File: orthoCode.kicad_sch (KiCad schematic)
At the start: 160 parts, among them K1:1 KEYSW, K1:10 KEYSW, K1:11 KEYSW, K1:12 KEYSW, K1:13 KEYSW, K1:14 KEYSW, K1:2 KEYSW, K1:3 KEYSW, K1:4 KEYSW, K1:5 KEYSW, K1:6 KEYSW, K1:7 KEYSW, K1:8 KEYSW, K1:9 KEYSW, K2:1 KEYSW, K2:10 KEYSW, K2:11 KEYSW, K2:13 KEYSW, K2:2 KEYSW, K2:3 KEYSW, K2:4 KEYSW, K2:5 KEYSW, K2:6 KEYSW, K2:7 KEYSW, K2:8 KEYSW, K2:9 KEYSW, K3:0 KEYSW, K3:1 KEYSW, K3:10 KEYSW, K3:11 KEYSW, K3:12 KEYSW, K3:13 KEYSW, K3:2 KEYSW, K3:3 KEYSW, K3:4 KEYSW, K3:5 KEYSW, K3:6 KEYSW, K3:7 KEYSW, K3:8 KEYSW, K3:9 KEYSW, K4:0 KEYSW, K4:1 KEYSW, K4:10 KEYSW, K4:11 KEYSW, K4:12 KEYSW, K4:13 KEYSW, K4:14 KEYSW, K4:2 KEYSW, K4:3 KEYSW, K4:4 KEYSW, K4:5 KEYSW, K4:6 KEYSW, K4:7 KEYSW, K4:8 KEYSW, K4:9 KEYSW, K5:0 KEYSW, K5:1 KEYSW, K5:10 KEYSW, K5:11 KEYSW, K5:12 KEYSW, K5:13 KEYSW, K5:14 KEYSW, K5:2 KEYSW, K5:3 KEYSW, K5:4 KEYSW, K5:5 KEYSW, K5:6 KEYSW, K5:7 KEYSW, K5:8 KEYSW, K5:9 KEYSW, U2 ATmega32U4-M, X1 Crystal

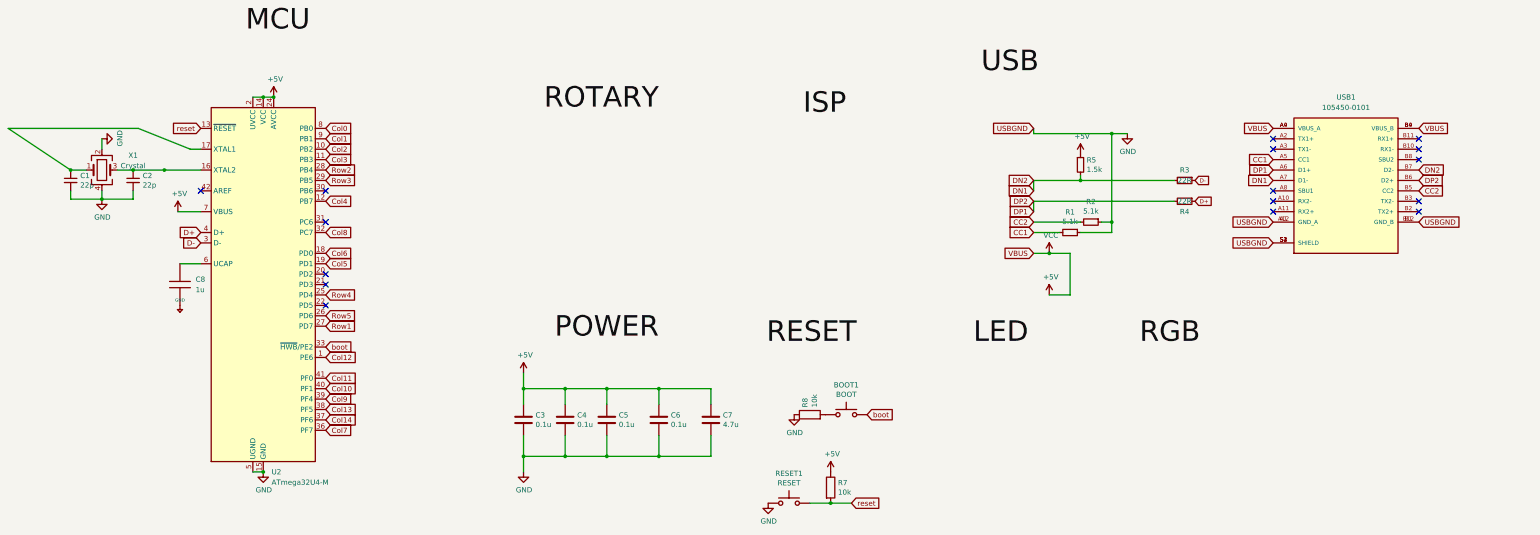
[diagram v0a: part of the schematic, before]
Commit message: switch to nicenano controller
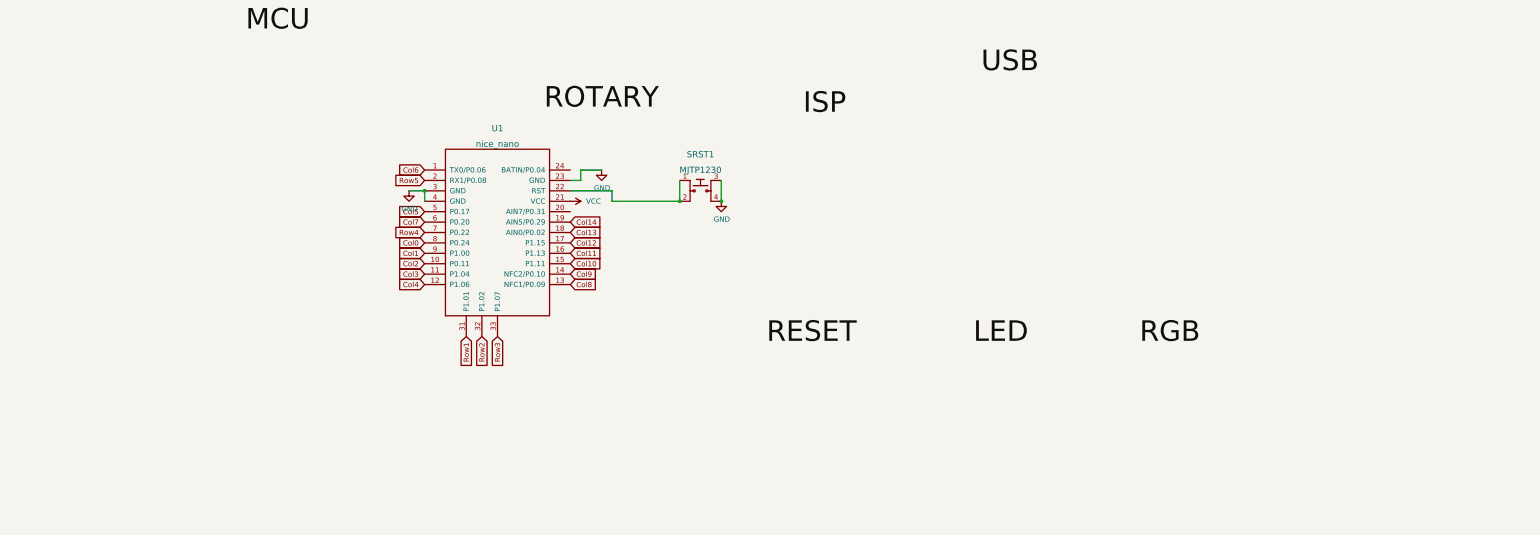
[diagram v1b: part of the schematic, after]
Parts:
- removed BOOT1: BOOT, cftkb:SW_PUSH_6mm, symbol Switch:SW_Push
- removed C1, C2: 22p, Capacitor_SMD:C_0805_2012Metric, symbol Device:C_Small
- removed C3, C4, C5, C6: 0.1u, Capacitor_SMD:C_0805_2012Metric, symbol Device:C
- removed C7: 4.7u, Capacitor_SMD:C_0805_2012Metric, symbol Device:C
- removed C8: 1u, Capacitor_SMD:C_0805_2012Metric, symbol keyboard:C
- removed R1, R2: 5.1k, Resistor_SMD:R_0805_2012Metric, symbol Device:R_Small
- removed R3, R4: 22R, Resistor_SMD:R_0805_2012Metric, symbol Device:R_Small
- removed R5: 1.5k, Resistor_SMD:R_0805_2012Metric, symbol Device:R_Small
- removed R7, R8: 10k, Resistor_SMD:R_0805_2012Metric, symbol Device:R
- removed RESET1: RESET, cftkb:SW_PUSH_6mm, symbol Switch:SW_Push
- removed U2: ATmega32U4-M, Package_DFN_QFN:QFN-44-1EP_7x7mm_P0.5mm_EP5.2x5.2mm, symbol MCU_Microchip_ATmega:ATmega32U4-M
- removed USB1: 105450-0101, 105450-0101:MOLEX_105450-0101, symbol 105450-0101:105450-0101
- removed X1: Crystal, Crystal:Crystal_SMD_3225-4Pin_3.2x2.5mm, symbol Device:Crystal_GND24
- added SRST1: MJTP1230, digikey-footprints:Switch_Tactile_THT_6x6mm_MJTP1230, symbol dk_Tactile-Switches:MJTP1230
- added U1: nice_nano, nice-nano-kicad-master:nice_nano, symbol nice_nano:nice_nano
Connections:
- net Col0: now also U1.8 (P0.24)
- net Col1: now also U1.9 (P1.00)
- net Col10: now also U1.15 (P1.11)
- net Col11: now also U1.16 (P1.13)
- net Col12: now also U1.17 (P1.15)
- net Col13: now also U1.18 (AIN0/P0.02)
- net Col14: now also U1.19 (AIN5/P0.29)
- net Col2: now also U1.10 (P0.11)
- net Col3: now also U1.11 (P1.04)
- net Col4: now also U1.12 (P1.06)
- net Col5: now also U1.5 (P0.17)
- net Col6: now also U1.1 (TX0/P0.06)
- net Col7: now also U1.6 (P0.20)
- net Col8: now also U1.13 (NFC1/P0.09)
- net Col9: now also U1.14 (NFC2/P0.10)
- net GND: now also SRST1.3, SRST1.4, U1.23 (GND), U1.3 (GND), U1.4 (GND)
- net Row1: now also U1.31 (P1.01)
- net Row2: now also U1.32 (P1.02)
- net Row3: now also U1.33 (P1.07)
- net Row4: now also U1.7 (P0.22)
- net Row5: now also U1.2 (RX1/P0.08)
- new net: SRST1.1, SRST1.2, U1.22 (RST)
- new net VCC: U1.21 (VCC)
- no-connect marks 16 -> 0
